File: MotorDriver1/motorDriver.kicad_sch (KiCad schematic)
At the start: 14 parts, among them J1 REPLACE W STM I/O PIN CONN, J2 REPLACE W STM I/O PIN CONN, Q1 IRLZ44N, Q2 IRLZ44N

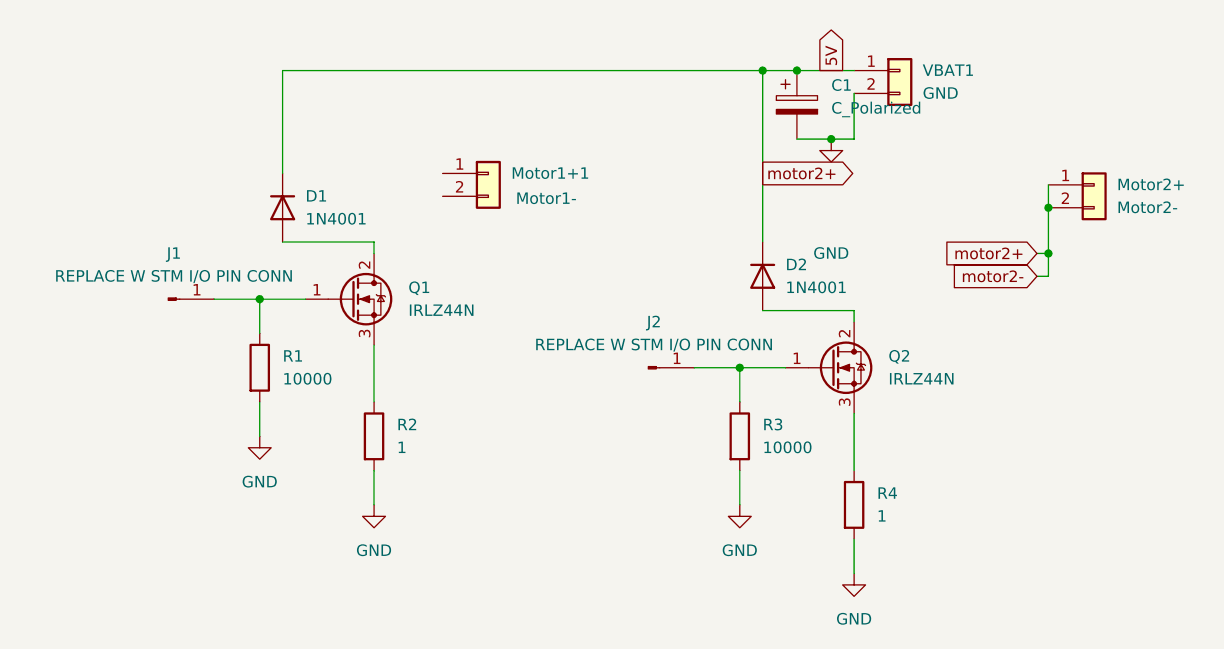
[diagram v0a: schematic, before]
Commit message: Added net labels and global lables to motor driver
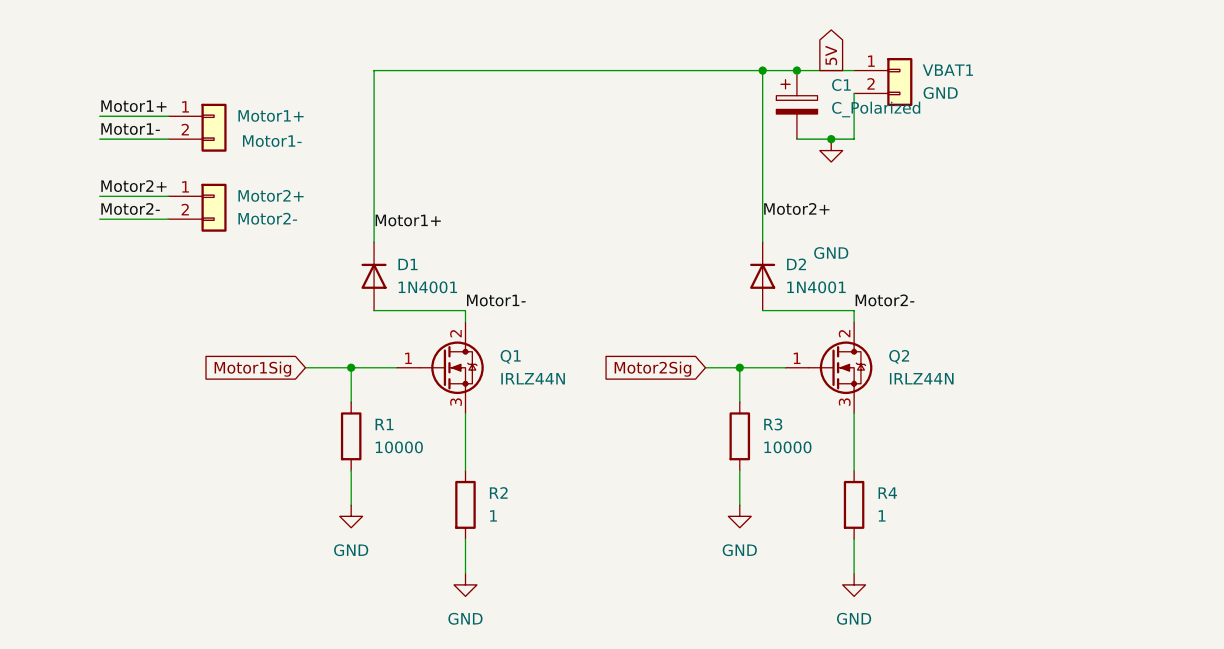
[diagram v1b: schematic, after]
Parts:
- removed J1, J2: REPLACE W STM I/O PIN CONN, symbol Connector:Conn_01x01_Pin
- renumbered Motor1+1 to Motor1+
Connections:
- net 5V: now also Motor1+.1 (Pin_1); no longer Motor2+.2 (Pin_2)
- net Motor1Sig: now reaches Q1.1 (G), R1.1
- net Motor1-: now reaches D1.2 (A), Q1.2 (D)
- net Motor1-: now also Motor1+.2 (Pin_2)
- net Motor2Sig: now reaches Q2.1 (G), R3.1
- net Motor2-: now reaches D2.2 (A), Q2.2 (D)
- net Motor2-: now also Motor2+.2 (Pin_2)
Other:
- moved on the sheet: D1, Motor1+, Motor2+, Q1, R1, R2

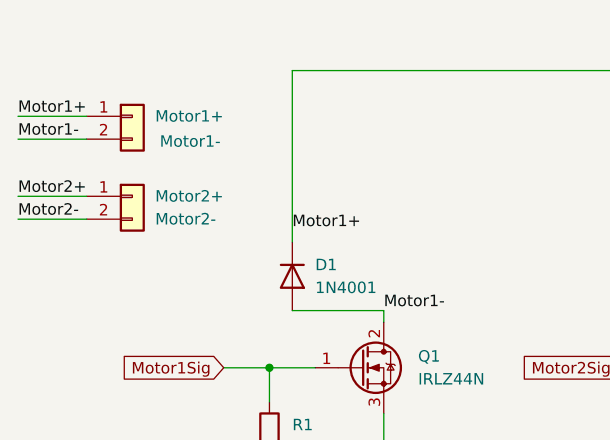
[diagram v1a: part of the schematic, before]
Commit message: added pressure sensor and flags to STM need op amp rails
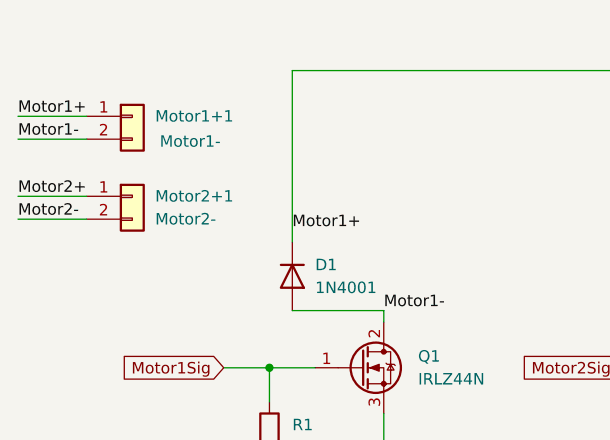
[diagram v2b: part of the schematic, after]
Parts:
- renumbered Motor1+ to Motor1+1, Motor2+ to Motor2+1
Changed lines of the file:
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@@
 		(on_board yes)
 		(dnp no)
-		(property "Reference" "#PWR?"
+		(property "Reference" "#PWR03"
 			(at 133.35 86.36 0)
 			(effects
@@
 		(dnp no)
 		(fields_autoplaced yes)
-		(property "Reference" "#PWR?"
+		(property "Reference" "#PWR01"
 			(at 92.71 134.62 0)
 			(effects
@@
 		(on_board yes)
 		(dnp no)
-		(property "Reference" "Motor1+"
+		(property "Reference" "Motor1+1"
 			(at 67.31 77.4699 0)
 			(effects
@@
 		(dnp no)
 		(fields_autoplaced yes)
-		(property "Reference" "Motor2+"
+		(property "Reference" "Motor2+1"
 			(at 67.31 86.3599 0)
 			(effects
@@
 			(project "MotorDriver1"
 				(path "/79cc9cfe-04d6-4d00-aa84-feae66cf8c45/bb18fbb4-ec68-4ac2-b714-52f61fe72a01"
-					(reference "Motor2+")
+					(reference "Motor2+1")
 					(unit 1)
 				)
@@
 		(dnp no)
 		(fields_autoplaced yes)
-		(property "Reference" "VBAT?"
+		(property "Reference" "VBAT1"
 			(at 143.51 72.3899 0)
 			(effects
@@
 		(dnp no)
 		(fields_autoplaced yes)
-		(property "Reference" "#PWR?"
+		(property "Reference" "#PWR06"
 			(at 135.89 134.62 0)
 			(effects
@@
 		(dnp no)
 		(fields_autoplaced yes)
-		(property "Reference" "#PWR?"
+		(property "Reference" "#PWR02"
 			(at 80.01 127 0)
 			(effects
@@
 		(dnp no)
 		(fields_autoplaced yes)
-		(property "Reference" "#PWR?"
+		(property "Reference" "#PWR04"
 			(at 123.19 127 0)
 			(effects

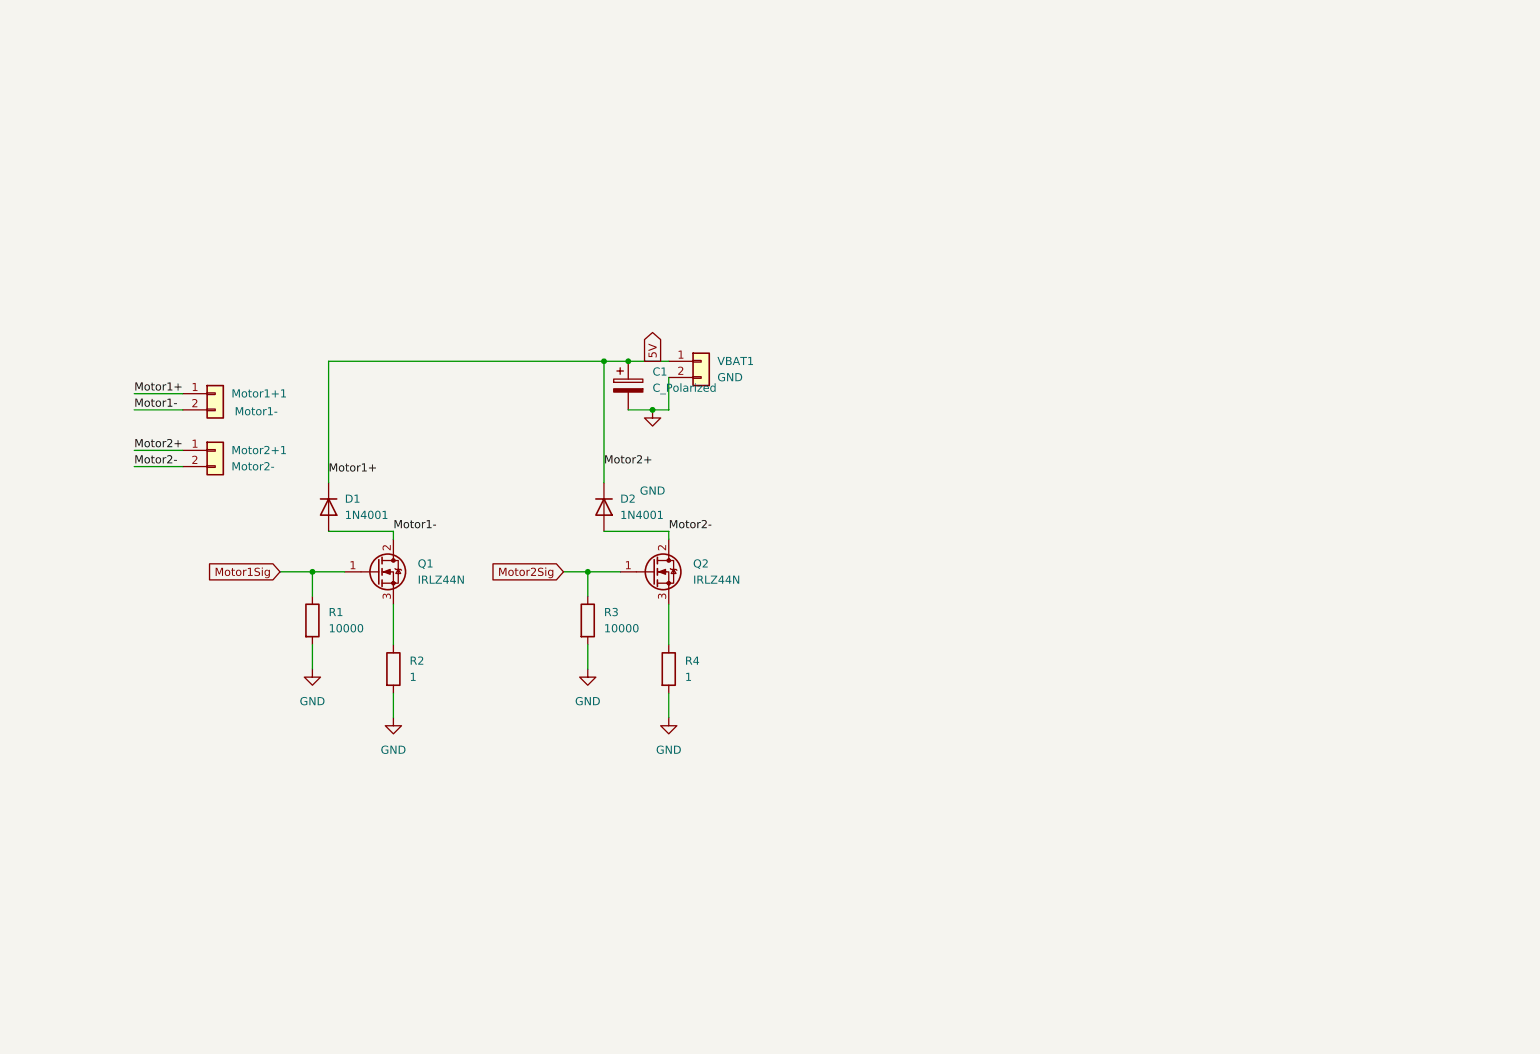
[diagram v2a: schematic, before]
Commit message: updated motor and sensor schematics and added footprints
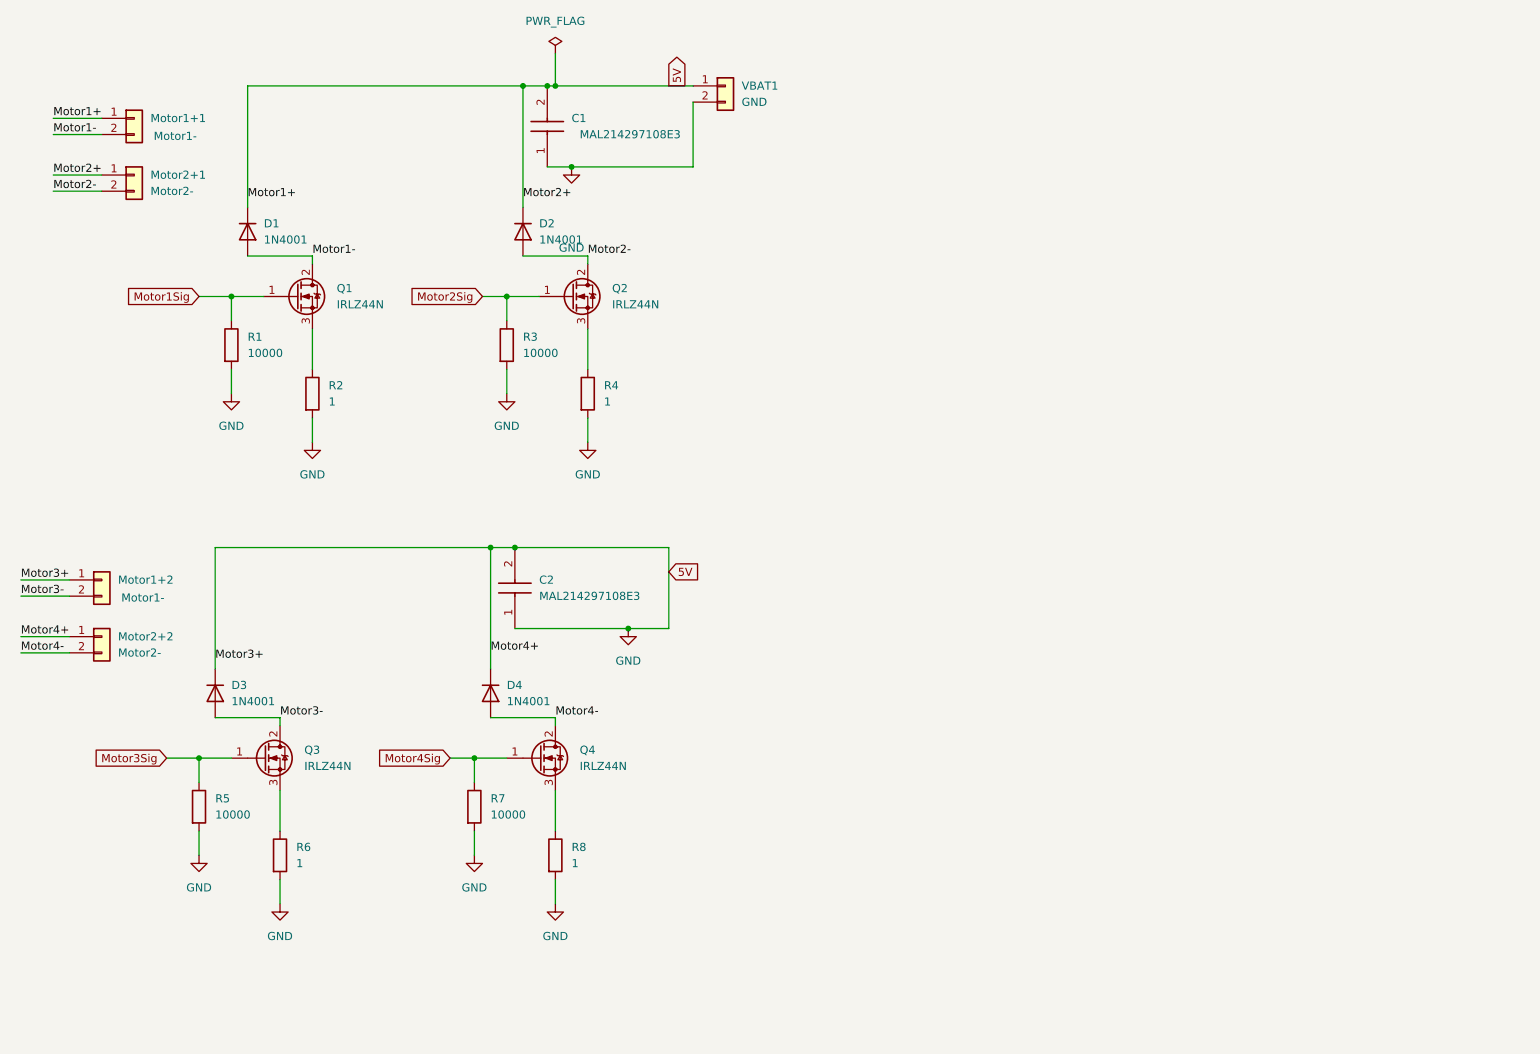
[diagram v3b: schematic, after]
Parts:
- removed C1: C_Polarized, symbol Device:C_Polarized
- added C1, C2: MAL214297108E3, footprintLib:CAPAE680X800N, symbol pcb:MAL214297108E3
- added D3, D4: 1N4001, Diode_THT:D_DO-41_SOD81_P10.16mm_Horizontal, symbol Diode:1N4001
- added Motor1+1: Motor1-, symbol Connector_Generic:Conn_01x02
- added Motor2+1: Motor2-, symbol Connector_Generic:Conn_01x02
- added Q3, Q4: IRLZ44N, Package_TO_SOT_THT:TO-220-3_Vertical, symbol Transistor_FET:IRLZ44N
- added R5, R7: 10000, symbol Device:R
- added R6, R8: 1, symbol Device:R
- renumbered Motor1+1 to Motor1+2, Motor2+1 to Motor2+2
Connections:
- net 5V is gone; now on net GND: D1.1 (K), D2.1 (K), Motor1+2.1 (Pin_1), Motor2+2.1 (Pin_1), VBAT1.1 (Pin_1)
- net GND: now also C1.1 (+), C1.2 (-), C2.1 (+), C2.2 (-), D3.1 (K), D4.1 (K), Motor1+1.1 (Pin_1), Motor2+1.1 (Pin_1), R5.2, R6.2, R7.2, R8.2
- net Motor1-: now also Motor1+1.2 (Pin_2); no longer Motor1+2.2 (Pin_2)
- net Motor2-: now also Motor2+1.2 (Pin_2); no longer Motor2+2.2 (Pin_2)
- new net: Q4.3 (S), R8.1
- new net: Q3.3 (S), R6.1
- new net Motor3-: D3.2 (A), Motor1+2.2 (Pin_2), Q3.2 (D)
- new net Motor3Sig: Q3.1 (G), R5.1
- new net Motor4-: D4.2 (A), Motor2+2.2 (Pin_2), Q4.2 (D)
- new net Motor4Sig: Q4.1 (G), R7.1
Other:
- moved on the sheet: D1, D2, Motor1+2, Motor2+2, Q1, Q2, R1, R2, R3, R4, VBAT1

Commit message: missing crystal verification
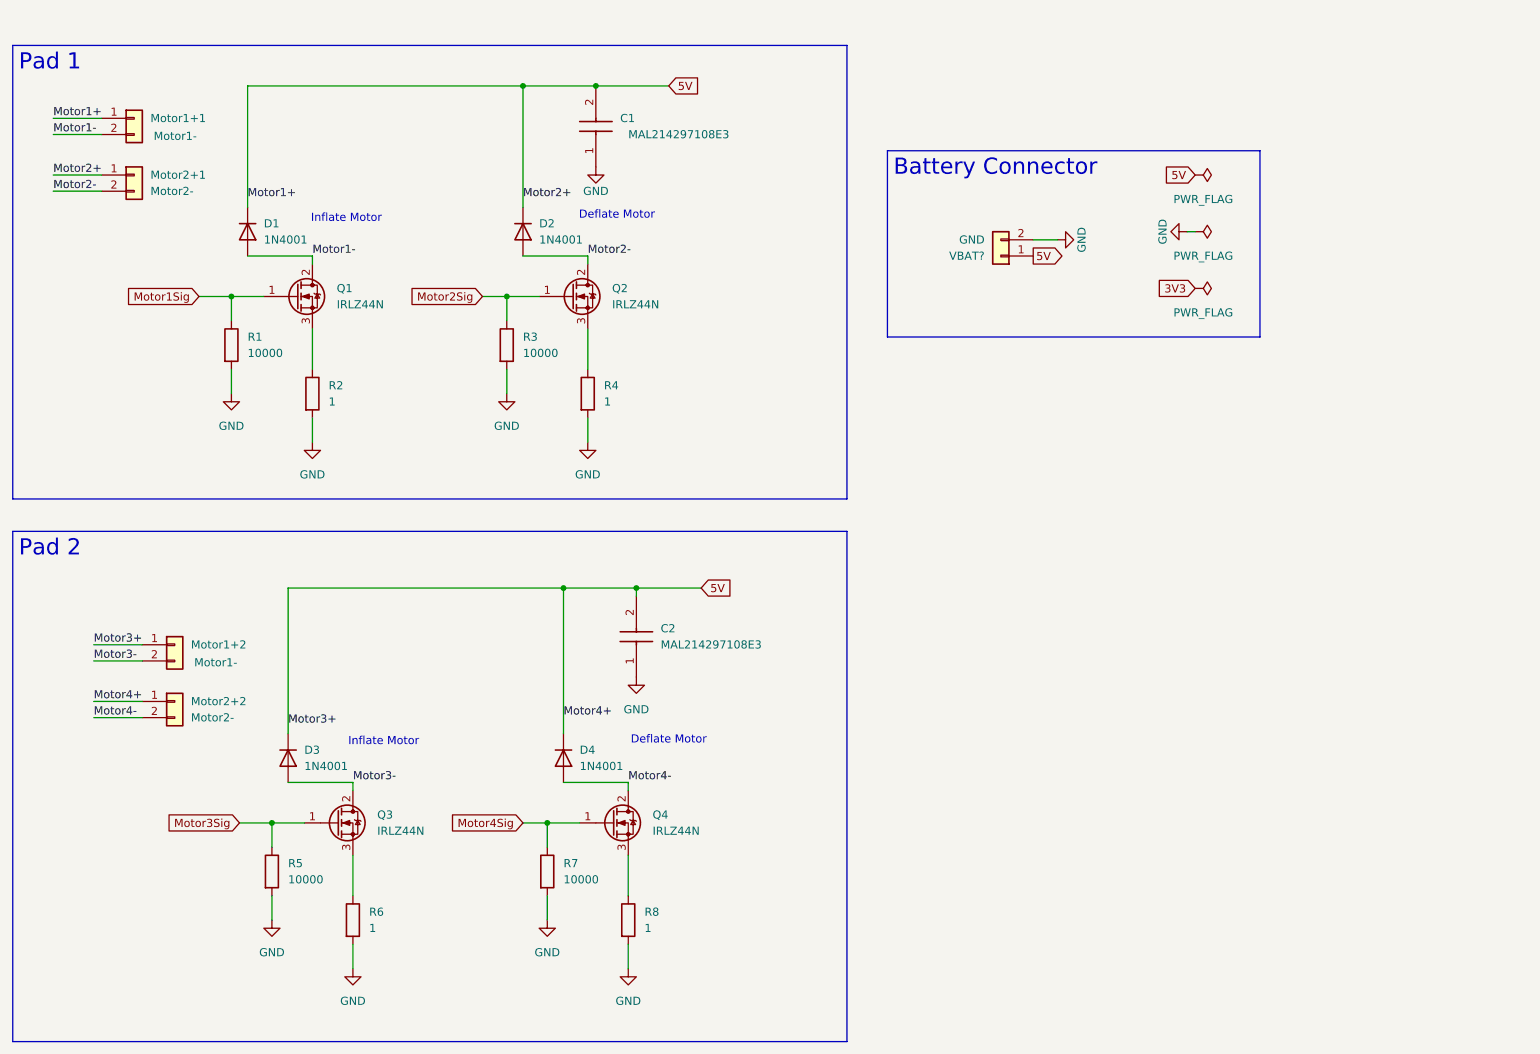
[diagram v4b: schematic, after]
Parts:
- renumbered VBAT1 to VBAT?
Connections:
- net GND: no longer C1.2 (-), C2.2 (-), D1.1 (K), D2.1 (K), D3.1 (K), D4.1 (K), Motor1+1.1 (Pin_1), Motor1+2.1 (Pin_1), Motor2+1.1 (Pin_1), Motor2+2.1 (Pin_1), VBAT?.1 (Pin_1)
- new net 5V: C1.2 (-), C2.2 (-), D1.1 (K), D2.1 (K), D3.1 (K), D4.1 (K), Motor1+1.1 (Pin_1), Motor1+2.1 (Pin_1), Motor2+1.1 (Pin_1), Motor2+2.1 (Pin_1), VBAT?.1 (Pin_1)
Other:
- note added: "Deflate Motor"
- note added: "Inflate Motor"
- moved on the sheet: C1, C2, D3, D4, Motor1+2, Motor2+2, Q3, Q4, R5, R6, R7, R8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

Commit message: Updated footprints
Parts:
- gave numbers to parts that had none: 1
- renumbered D3 to D2, D2 to D3, Q3 to Q2, Q2 to Q3, R5 to R2, R2 to R3, R6 to R4, R3 to R5, R7 to R6, R4 to R7
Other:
- moved on the sheet: VBAT1
